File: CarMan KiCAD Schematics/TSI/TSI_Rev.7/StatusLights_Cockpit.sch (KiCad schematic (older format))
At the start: 17 parts, among them SW4 RTDS Test, U1 RDE03110S12, U11 TLP293, U13 TLP293, U43 NCD9830DBR2G

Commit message: TSI Should be final schematic
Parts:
- added C52, C53: 0.1u, Capacitor_SMD:C_0805_2012Metric_Pad1.18x1.45mm_HandSolder, symbol Device:C
- added R113, R114: 10K, Resistor_SMD:R_0805_2012Metric_Pad1.20x1.40mm_HandSolder, symbol Device:R
- added U46: SI8600AB-B-IS, TSI_Rev_2021_Footprint_Lib:SOIC127P600X175-8N, symbol CarMan_KiCAD_Library:SI8600AB-B-IS
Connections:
- net labels added: SCL_5V, SDA_5V
- wire segments 93 -> 117
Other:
- note added: "I2C Isolator\n"
- note added: "Isolator is required because the Ref_In must\n be equal to the max value of the analog inputs \nand cannot be greater than by VDD. At the same\ntime, however, SDA and SCL are considered high \nif they are > 0.7*VDD. Since SDA and SCL \nare 3.3V, they would never be considered high."
- moved on the sheet: D1, R15, R3, R99, U11, U43

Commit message: Pre-review_schematic
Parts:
- C17, C6: footprint Capacitor_SMD:C_0805_2012Metric_Pad1.15x1.40mm_HandSolder -> Capacitor_SMD:C_0805_2012Metric_Pad1.18x1.45mm_HandSolder
- R12, R15, R3, R68, R74, R97, R99: footprint Resistor_SMD:R_0805_2012Metric_Pad1.15x1.40mm_HandSolder -> Resistor_SMD:R_0805_2012Metric_Pad1.20x1.40mm_HandSolder
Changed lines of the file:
@@
 F 0 "R3" H 5500 1425 50  0000 C CNN
 F 1 "2.4K" V 5600 1425 50  0000 C CNN
-F 2 "Resistor_SMD:R_0805_2012Metric_Pad1.15x1.40mm_HandSolder" V 5530 1425 50  0001 C CNN
+F 2 "Resistor_SMD:R_0805_2012Metric_Pad1.20x1.40mm_HandSolder" V 5530 1425 50  0001 C CNN
 F 3 "~" H 5600 1425 50  0001 C CNN
 	1    5600 1425
@@
 F 0 "R15" V 3175 1775 50  0000 C CNN
 F 1 "300" V 3275 1775 50  0000 C CNN
-F 2 "Resistor_SMD:R_0805_2012Metric_Pad1.15x1.40mm_HandSolder" V 3205 1775 50  0001 C CNN
+F 2 "Resistor_SMD:R_0805_2012Metric_Pad1.20x1.40mm_HandSolder" V 3205 1775 50  0001 C CNN
 F 3 "~" H 3275 1775 50  0001 C CNN
 	1    3275 1775
@@
 F 0 "C17" H 4578 6746 50  0000 L CNN
 F 1 "4.7u" H 4578 6655 50  0000 L CNN
-F 2 "Capacitor_SMD:C_0805_2012Metric_Pad1.15x1.40mm_HandSolder" H 4400 6700 50  0001 C CNN
+F 2 "Capacitor_SMD:C_0805_2012Metric_Pad1.18x1.45mm_HandSolder" H 4400 6700 50  0001 C CNN
 F 3 "~" H 4400 6700 50  0001 C CNN
 	1    4400 6700
@@
 F 0 "C6" H 9075 5800 50  0000 L CNN
 F 1 "0.1u" H 9075 5600 50  0000 L CNN
-F 2 "Capacitor_SMD:C_0805_2012Metric_Pad1.15x1.40mm_HandSolder" H 9025 5700 50  0001 C CNN
+F 2 "Capacitor_SMD:C_0805_2012Metric_Pad1.18x1.45mm_HandSolder" H 9025 5700 50  0001 C CNN
 F 3 "~" H 9025 5700 50  0001 C CNN
 	1    9025 5700
@@
 F 0 "R97" V 8175 6125 50  0000 C CNN
 F 1 "10K" V 8275 6125 50  0000 C CNN
-F 2 "Resistor_SMD:R_0805_2012Metric_Pad1.15x1.40mm_HandSolder" V 8205 6125 50  0001 C CNN
+F 2 "Resistor_SMD:R_0805_2012Metric_Pad1.20x1.40mm_HandSolder" V 8205 6125 50  0001 C CNN
 F 3 "~" H 8275 6125 50  0001 C CNN
 	1    8275 6125
@@
 F 0 "R74" V 2575 4450 50  0000 C CNN
 F 1 "10K" V 2675 4450 50  0000 C CNN
-F 2 "Resistor_SMD:R_0805_2012Metric_Pad1.15x1.40mm_HandSolder" V 2605 4450 50  0001 C CNN
+F 2 "Resistor_SMD:R_0805_2012Metric_Pad1.20x1.40mm_HandSolder" V 2605 4450 50  0001 C CNN
 F 3 "~" H 2675 4450 50  0001 C CNN
 	1    2675 4450
@@
 F 0 "R12" V 1375 4025 50  0000 C CNN
 F 1 "120" V 1475 4025 50  0000 C CNN
-F 2 "Resistor_SMD:R_0805_2012Metric_Pad1.15x1.40mm_HandSolder" V 1405 4025 50  0001 C CNN
+F 2 "Resistor_SMD:R_0805_2012Metric_Pad1.20x1.40mm_HandSolder" V 1405 4025 50  0001 C CNN
 F 3 "~" H 1475 4025 50  0001 C CNN
 	1    1475 4025
@@
 F 0 "R68" V 7900 5900 50  0000 C CNN
 F 1 "10K" V 8000 5900 50  0000 C CNN
-F 2 "Resistor_SMD:R_0805_2012Metric_Pad1.15x1.40mm_HandSolder" V 7930 5900 50  0001 C CNN
+F 2 "Resistor_SMD:R_0805_2012Metric_Pad1.20x1.40mm_HandSolder" V 7930 5900 50  0001 C CNN
 F 3 "~" H 8000 5900 50  0001 C CNN
 	1    8000 5900
@@
 F 0 "R99" V 4200 2175 50  0000 C CNN
 F 1 "1K" V 4300 2175 50  0000 C CNN
-F 2 "Resistor_SMD:R_0805_2012Metric_Pad1.15x1.40mm_HandSolder" V 4230 2175 50  0001 C CNN
+F 2 "Resistor_SMD:R_0805_2012Metric_Pad1.20x1.40mm_HandSolder" V 4230 2175 50  0001 C CNN
 F 3 "~" H 4300 2175 50  0001 C CNN
 	1    4300 2175

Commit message: TSI Post-Nadovich
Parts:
- R113, R114: value 10K -> 4.7K
- R68: value 10K -> 100K
- R97: value 10K -> 1K
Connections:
- net labels added: Drive_BTN_LOGIC
- wire segments 117 -> 120
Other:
- note added: "RTDS\n(J18)\n"
- note removed: "Brake Light & RTDS\n(J18)\n"
- moved on the sheet: C6, R68, R97
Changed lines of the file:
@@
 Text Notes 2800 5900 0    50   ~ 0
 HIGH VOLTAGE\n
-Text Label 10125 6125 2    50   ~ 0
+Text Label 9450 6075 2    50   ~ 0
 Drive_BTN_RTN
-Text HLabel 1250 2500 0    50   Output ~ 0
+Text HLabel 1250 2600 0    50   Output ~ 0
 TSAL
+Text HLabel 1250 2800 0    50   Output ~ 0
+TSAL_RTN
+Text Label 1950 2600 2    50   ~ 0
+TSAL
+Text Label 1950 2800 2    50   ~ 0
+TSAL_RTN
 Text HLabel 1250 2700 0    50   Output ~ 0
-TSAL_RTN
-Text Label 1950 2500 2    50   ~ 0
-TSAL
+TSAL_Cockpit
 Text Label 1950 2700 2    50   ~ 0
-TSAL_RTN
-Text HLabel 1250 2600 0    50   Output ~ 0
-TSAL_Cockpit
-Text Label 1950 2600 2    50   ~ 0
 TSAL_Cockpit
 Text Label 5600 2475 2    50   ~ 0
@@
 Text Notes 7025 6925 0    157  ~ 0
 STATUS LIGHTS, TSAL, RTDS & ADC
-Text HLabel 1250 2300 0    50   Output ~ 0
-RTDS
-Text Label 1950 2300 2    50   ~ 0
+Text HLabel 1250 2400 0    50   Output ~ 0
 RTDS
 Text Label 1950 2400 2    50   ~ 0
+RTDS
+Text Label 1950 2500 2    50   ~ 0
 RTDS_RTN
-Text HLabel 1250 2400 0    50   Output ~ 0
+Text HLabel 1250 2500 0    50   Output ~ 0
 RTDS_RTN
 Text Notes 675  650  0    79   ~ 0
  LOW VOLTAGE SIGNALS\n
-Text HLabel 1250 2200 0    50   Output ~ 0
+Text HLabel 1250 2300 0    50   Output ~ 0
 Drive_LED
-Text Label 1950 2200 2    50   ~ 0
+Text Label 1950 2300 2    50   ~ 0
 Drive_LED
 Text Label 5600 6400 2    50   ~ 0
@@
 Wire Wire Line
 	5000 6400 5600 6400
-Text Label 9200 6125 0    50   ~ 0
+Text Label 8500 6075 0    50   ~ 0
 GLV_RTN
 $Comp
 L TSI_Rev.5-rescue:CAP-pspice C6
 U 1 1 5FBC364D
-P 9025 5700
-F 0 "C6" H 9075 5800 50  0000 L CNN
-F 1 "0.1u" H 9075 5600 50  0000 L CNN
-F 2 "Capacitor_SMD:C_0805_2012Metric_Pad1.18x1.45mm_HandSolder" H 9025 5700 50  0001 C CNN
-F 3 "~" H 9025 5700 50  0001 C CNN
-	1    9025 5700
-	0    1    1    0
-$EndComp
-Text Label 8825 6125 2    50   ~ 0
-Drive_BTN
-$Comp
-L TSI_Rev.5-rescue:R-Device R97
-U 1 1 5FA84F23
-P 8275 6125
-F 0 "R97" V 8175 6125 50  0000 C CNN
-F 1 "10K" V 8275 6125 50  0000 C CNN
-F 2 "Resistor_SMD:R_0805_2012Metric_Pad1.20x1.40mm_HandSolder" V 8205 6125 50  0001 C CNN
-F 3 "~" H 8275 6125 50  0001 C CNN
-	1    8275 6125
-	0    -1   1    0
+P 9775 5750
+F 0 "C6" H 9825 5850 50  0000 L CNN
+F 1 "0.1u" H 9825 5650 50  0000 L CNN
+F 2 "Capacitor_SMD:C_0805_2012Metric_Pad1.18x1.45mm_HandSolder" H 9775 5750 50  0001 C CNN
+F 3 "~" H 9775 5750 50  0001 C CNN
+	1    9775 5750
+	1    0    0    -1
 $EndComp
 Wire Wire Line
@@
 	1250 1275 1950 1275
 Wire Wire Line
-	1250 2200 1950 2200
+	1250 2300 1950 2300
 Wire Wire Line
 	1250 1175 1950 1175
@@
 	1250 1475 1950 1475
 Wire Wire Line
-	1250 2300 1950 2300
-Wire Wire Line
 	1250 2400 1950 2400
 Wire Wire Line
+	1250 2500 1950 2500
+Wire Wire Line
 	1250 775  1950 775
 Wire Wire Line
@@
 	1250 1075 1950 1075
 Wire Wire Line
-	1250 2500 1950 2500
-Wire Wire Line
 	1250 2600 1950 2600
 Wire Wire Line
 	1250 2700 1950 2700
+Wire Wire Line
+	1250 2800 1950 2800
 Wire Notes Line
 	500  500  2250 500
@@
 L TSI_Rev.5-rescue:R-Device R68
 U 1 1 5FA84662
-P 8000 5900
-F 0 "R68" V 7900 5900 50  0000 C CNN
-F 1 "10K" V 8000 5900 50  0000 C CNN
-F 2 "Resistor_SMD:R_0805_2012Metric_Pad1.20x1.40mm_HandSolder" V 7930 5900 50  0001 C CNN
-F 3 "~" H 8000 5900 50  0001 C CNN
-	1    8000 5900
+P 7725 5275
+F 0 "R68" V 7800 5275 50  0000 C CNN
+F 1 "100K" V 7725 5275 50  0000 C CNN
+F 2 "Resistor_SMD:R_0805_2012Metric_Pad1.20x1.40mm_HandSolder" V 7655 5275 50  0001 C CNN
+F 3 "~" H 7725 5275 50  0001 C CNN
+	1    7725 5275
 	-1   0    0    1
 $EndComp
-Text Label 8000 5700 0    50   ~ 0
-5V
-Text Notes 9200 6400 2    50   ~ 0
+Text Label 7725 5075 0    50   ~ 0
+3.3V
+Text Notes 8500 6350 2    50   ~ 0
 COCKPIT\n(J9)\n
 $Comp
@@
 	2675 4225 3675 4225
 Text Notes 3600 4500 2    43   ~ 0
-Brake Light & RTDS\n(J18)\n
+RTDS\n(J18)\n
 Wire Wire Line
 	3050 825  3450 825
@@
 GLV_RTN
 Wire Wire Line
-	8000 5700 8000 5750
+	7725 5075 7725 5125
 Wire Wire Line
 	4300 2375 4775 2375
@@
 	3850 7000 4400 7000
 Wire Wire Line
-	8000 6050 8000 6125
-Wire Wire Line
-	10150 5700 10150 6125
-Wire Notes Line
-	9175 6025 8850 6025
-Wire Notes Line
-	8850 6025 8850 6225
-Wire Notes Line
-	9175 6025 9175 6225
-Wire Notes Line
-	8850 6225 9175 6225
-Wire Notes Line
-	6975 6475 7550 6475
-Wire Notes Line
-	7625 6475 11175 6475
-Wire Notes Line
-	11175 6475 11175 5275
-Wire Notes Line
-	6975 5275 6975 6475
-Wire Notes Line
-	6975 5250 11175 5250
-Text Notes 8625 5400 0    79   ~ 0
+	7725 5425 7725 5500
+Wire Wire Line
+	9775 6000 10200 6000
+Wire Notes Line
+	8475 5975 8150 5975
+Wire Notes Line
+	8150 5975 8150 6175
+Wire Notes Line
+	8475 5975 8475 6175
+Wire Notes Line
+	8150 6175 8475 6175
+Text Notes 8700 4975 0    79   ~ 0
 DRIVE BUTTON
-Text HLabel 1250 1875 0    50   Input ~ 0
+Text HLabel 1250 1975 0    50   Input ~ 0
 SDA
-Text Label 1950 1875 2    50   ~ 0
+Text Label 1950 1975 2    50   ~ 0
 SDA
 Wire Wire Line
-	1250 1875 1950 1875
-Text HLabel 1250 1975 0    50   Input ~ 0
+	1250 1975 1950 1975
+Text HLabel 1250 2075 0    50   Input ~ 0
 SCL
 Wire Wire Line
-	1250 1975 1950 1975
-Text Label 1950 1975 2    50   ~ 0
+	1250 2075 1950 2075
+Text Label 1950 2075 2    50   ~ 0
 SCL
 Wire Notes Line
-	2250 500  2250 2800
-Wire Notes Line
-	2250 2800 500  2800
-Wire Notes Line
-	500  500  500  2800
+	2250 2900 500  2900
 Wire Wire Line
 	5550 4025 6150 4025
@@
 Wire Wire Line
 	10175 2400 11000 2400
-Text Label 9450 775  0    39   ~ 0
+Text Label 10350 775  2    39   ~ 0
 GLV_RTN
 NoConn ~ 10175 1500
@@
 	10350 1350 10350 775
 Wire Wire Line
-	10350 775  8725 775
-Wire Wire Line
 	8725 775  8725 1500
 Wire Wire Line
 	8725 1500 8925 1500
 Wire Wire Line
-	8000 6125 8125 6125
-Wire Wire Line
-	9100 6125 10150 6125
-Wire Wire Line
-	9275 5700 10150 5700
-Wire Wire Line
-	8000 5700 8775 5700
-Wire Wire Line
-	8425 6125 8925 6125
-Text HLabel 1250 1675 0    50   Input ~ 0
+	8400 6075 9450 6075
+Text HLabel 1250 1775 0    50   Input ~ 0
 CoolTemp
-Text Label 1950 1675 2    50   ~ 0
+Text Label 1950 1775 2    50   ~ 0
 CoolTemp
 Wire Wire Line
-	1250 1675 1950 1675
-Text HLabel 1250 1775 0    50   Input ~ 0
+	1250 1775 1950 1775
+Text HLabel 1250 1875 0    50   Input ~ 0
 APPS
-Text Label 1950 1775 2    50   ~ 0
+Text Label 1950 1875 2    50   ~ 0
 APPS
 Wire Wire Line
-	1250 1775 1950 1775
+	1250 1875 1950 1875
 Wire Wire Line
 	8550 3850 8500 3850
@@
 P 8000 2700
 F 0 "R114" V 7793 2700 50  0000 C CNN
-F 1 "10K" V 7884 2700 50  0000 C CNN
+F 1 "4.7K" V 7884 2700 50  0000 C CNN
 F 2 "Resistor_SMD:R_0805_2012Metric_Pad1.20x1.40mm_HandSolder" V 7930 2700 50  0001 C CNN
 F 3 "~" H 8000 2700 50  0001 C CNN
@@
 P 7150 2700
 F 0 "R113" V 6943 2700 50  0000 C CNN
-F 1 "10K" V 7034 2700 50  0000 C CNN
+F 1 "4.7K" V 7034 2700 50  0000 C CNN
 F 2 "Resistor_SMD:R_0805_2012Metric_Pad1.20x1.40mm_HandSolder" V 7080 2700 50  0001 C CNN
 F 3 "~" H 7150 2700 50  0001 C CNN
@@
 Wire Wire Line
 	9550 3100 9550 3300
+Text Label 8725 775  0    39   ~ 0
+GLV_RTN
+Wire Notes Line
+	6975 6475 11175 6475
+Wire Wire Line
+	7725 6075 8225 6075
+$Comp
+L TSI_Rev.5-rescue:R-Device R97
+U 1 1 5FA84F23
+P 7725 5750
+F 0 "R97" V 7650 5750 50  0000 C CNN
+F 1 "1K" V 7725 5750 50  0000 C CNN
+F 2 "Resistor_SMD:R_0805_2012Metric_Pad1.20x1.40mm_HandSolder" V 7655 5750 50  0001 C CNN
+F 3 "~" H 7725 5750 50  0001 C CNN
+	1    7725 5750
+	1    0    0    1
+$EndComp
+Text Label 8125 6075 2    50   ~ 0
+Drive_BTN
+Wire Wire Line
+	7725 5900 7725 6075
+Wire Wire Line
+	7725 5600 7725 5500
+Connection ~ 7725 5500
+Wire Wire Line
+	7725 5500 9775 5500
+Text Label 10200 6000 2    39   ~ 0
+GLV_RTN
+Text Label 10325 5500 0    39   ~ 0
+Drive_BTN_LOGIC
+Wire Wire Line
+	9775 5500 10325 5500
+Connection ~ 9775 5500
+Wire Notes Line
+	11175 4750 11175 6475
+Wire Notes Line
+	6975 4750 6975 6475
+Wire Notes Line
+	11175 4750 6975 4750
+Text HLabel 1250 2200 0    50   Output ~ 0
+Drive_BTN_LOGIC
+Text Label 1950 2200 2    50   ~ 0
+Drive_BTN_LOGIC
+Wire Wire Line
+	1250 2200 1950 2200
+Text HLabel 1250 1575 0    50   Input ~ 0
+SDA_5V
+Text HLabel 1250 1675 0    50   Input ~ 0
+SCL_5V
+Text Label 1950 1575 2    50   ~ 0
+SDA_5V
+Text Label 1950 1675 2    50   ~ 0
+SCL_5V
+Wire Wire Line
+	1250 1575 1950 1575
+Wire Wire Line
+	1250 1675 1950 1675
+Wire Notes Line
+	2250 500  2250 2900
+Wire Notes Line
+	500  500  500  2900
 $EndSCHEMATC

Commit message: TSI REV7 Final Schematic before Layout
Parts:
- removed TP12: TSAL_LV, TestPoint:TestPoint_Pad_D3.0mm, symbol TSI_Rev.5-rescue:TestPoint-Connector
- added J26: TSAL_LV TP, Connector_PinSocket_2.54mm:PinSocket_1x01_P2.54mm_Vertical, symbol Connector_Generic:Conn_01x02
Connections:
- wire segments 120 -> 122
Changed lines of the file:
@@
 Text Label 5600 7000 2    50   ~ 0
 TSAL_RTN
-$Comp
-L TSI_Rev.5-rescue:TestPoint-Connector TP12
-U 1 1 5FA80FFC
-P 4200 6200
-F 0 "TP12" H 4258 6318 50  0000 L CNN
-F 1 "TSAL_LV" H 4258 6227 50  0000 L CNN
-F 2 "TestPoint:TestPoint_Pad_D3.0mm" H 4400 6200 50  0001 C CNN
-F 3 "~" H 4400 6200 50  0001 C CNN
-	1    4200 6200
-	1    0    0    -1
-$EndComp
 Text Notes 2800 5900 0    50   ~ 0
 HIGH VOLTAGE\n
@@
 Wire Notes Line
 	500  500  500  2900
+$Comp
+L Connector_Generic:Conn_01x02 J26
+U 1 1 624D7528
+P 4200 6000
+F 0 "J26" V 4350 5950 50  0000 R CNN
+F 1 "TSAL_LV TP" V 4200 5800 50  0000 R CNN
+F 2 "Connector_PinSocket_2.54mm:PinSocket_1x01_P2.54mm_Vertical" H 4200 6000 50  0001 C CNN
+F 3 "~" H 4200 6000 50  0001 C CNN
+	1    4200 6000
+	0    -1   -1   0
+$EndComp
+Wire Wire Line
+	4300 6200 4300 6250
+Wire Wire Line
+	4300 6250 4650 6250
+Text Label 4650 6250 2    39   ~ 0
+GLV_RTN
 $EndSCHEMATC

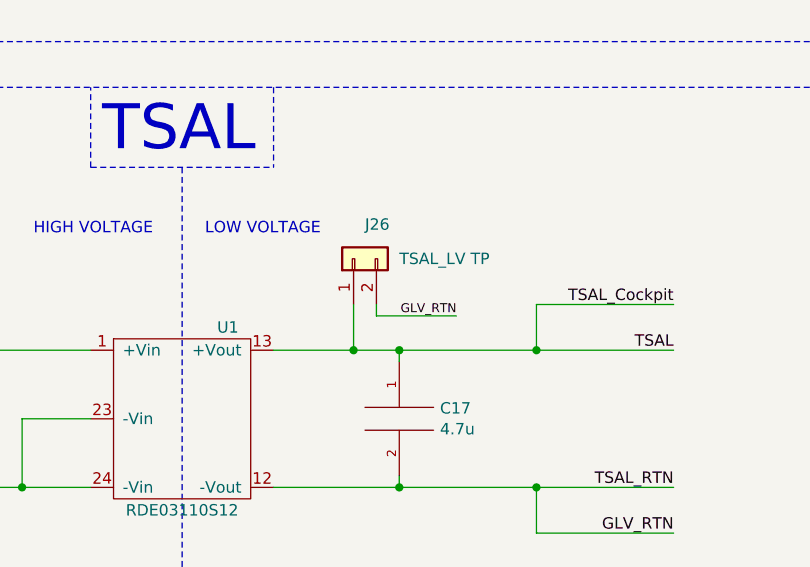
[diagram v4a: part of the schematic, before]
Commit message: Updated Schematic and removed extra footprints from PCB. Ready to begin routing new elements in.
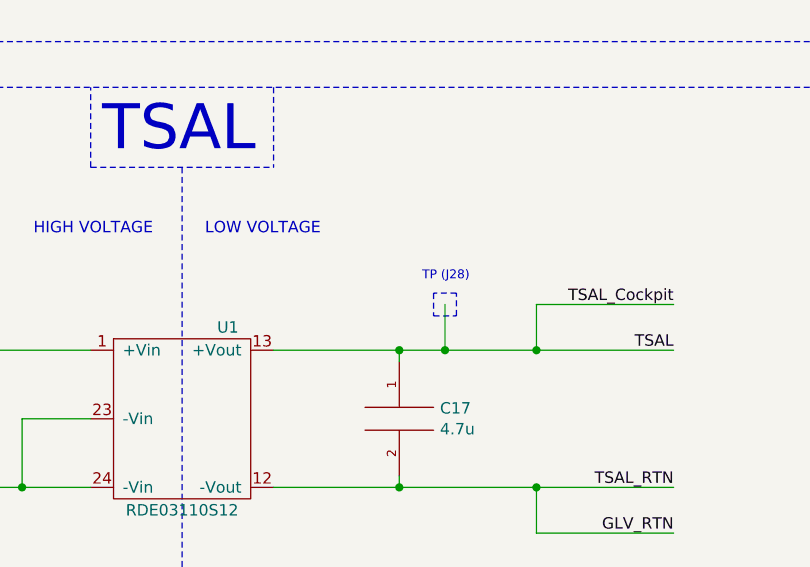
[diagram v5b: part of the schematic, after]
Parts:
- removed J26: TSAL_LV TP, Connector_PinSocket_2.54mm:PinSocket_1x01_P2.54mm_Vertical, symbol Connector_Generic:Conn_01x02
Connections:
- wire segments 122 -> 120
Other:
- note added: "TP (J28)"
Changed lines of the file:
@@
 HV-
-Wire Wire Line
-	3850 6400 4200 6400
 Wire Wire Line
 	5000 6400 5000 6200
@@
 Connection ~ 4400 6400
 Wire Wire Line
-	4400 6400 5000 6400
+	4400 6400 4600 6400
 Wire Wire Line
 	4400 6950 4400 7000
 Connection ~ 4400 7000
-Wire Wire Line
-	4200 6400 4200 6200
-Connection ~ 4200 6400
-Wire Wire Line
-	4200 6400 4400 6400
 Text Label 5600 7000 2    50   ~ 0
 TSAL_RTN
@@
 Wire Notes Line
 	500  500  500  2900
-$Comp
-L Connector_Generic:Conn_01x02 J26
-U 1 1 624D7528
-P 4200 6000
-F 0 "J26" V 4350 5950 50  0000 R CNN
-F 1 "TSAL_LV TP" V 4200 5800 50  0000 R CNN
-F 2 "Connector_PinSocket_2.54mm:PinSocket_1x01_P2.54mm_Vertical" H 4200 6000 50  0001 C CNN
-F 3 "~" H 4200 6000 50  0001 C CNN
-	1    4200 6000
-	0    -1   -1   0
-$EndComp
-Wire Wire Line
-	4300 6200 4300 6250
-Wire Wire Line
-	4300 6250 4650 6250
-Text Label 4650 6250 2    39   ~ 0
-GLV_RTN
+Wire Wire Line
+	3850 6400 4400 6400
+Wire Wire Line
+	4600 6400 4600 6200
+Connection ~ 4600 6400
+Wire Wire Line
+	4600 6400 5000 6400
+Wire Notes Line
+	4550 6150 4550 6250
+Wire Notes Line
+	4550 6250 4650 6250
+Wire Notes Line
+	4650 6250 4650 6150
+Wire Notes Line
+	4650 6150 4550 6150
+Text Notes 4500 6100 0    39   ~ 0
+TP (J28)
 $EndSCHEMATC
